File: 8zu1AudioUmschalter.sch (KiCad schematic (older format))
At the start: 56 parts, among them IC1 ATMEGA8A-A, IC2 MAX9890, J1 USB, J2 LUM 1503-07, J3 LUM 1503-07, J4 LUM 1503-07, J5 LUM 1503-07, J6 LUM 1503-07, J7 LUM 1503-07, J8 LUM 1503-07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

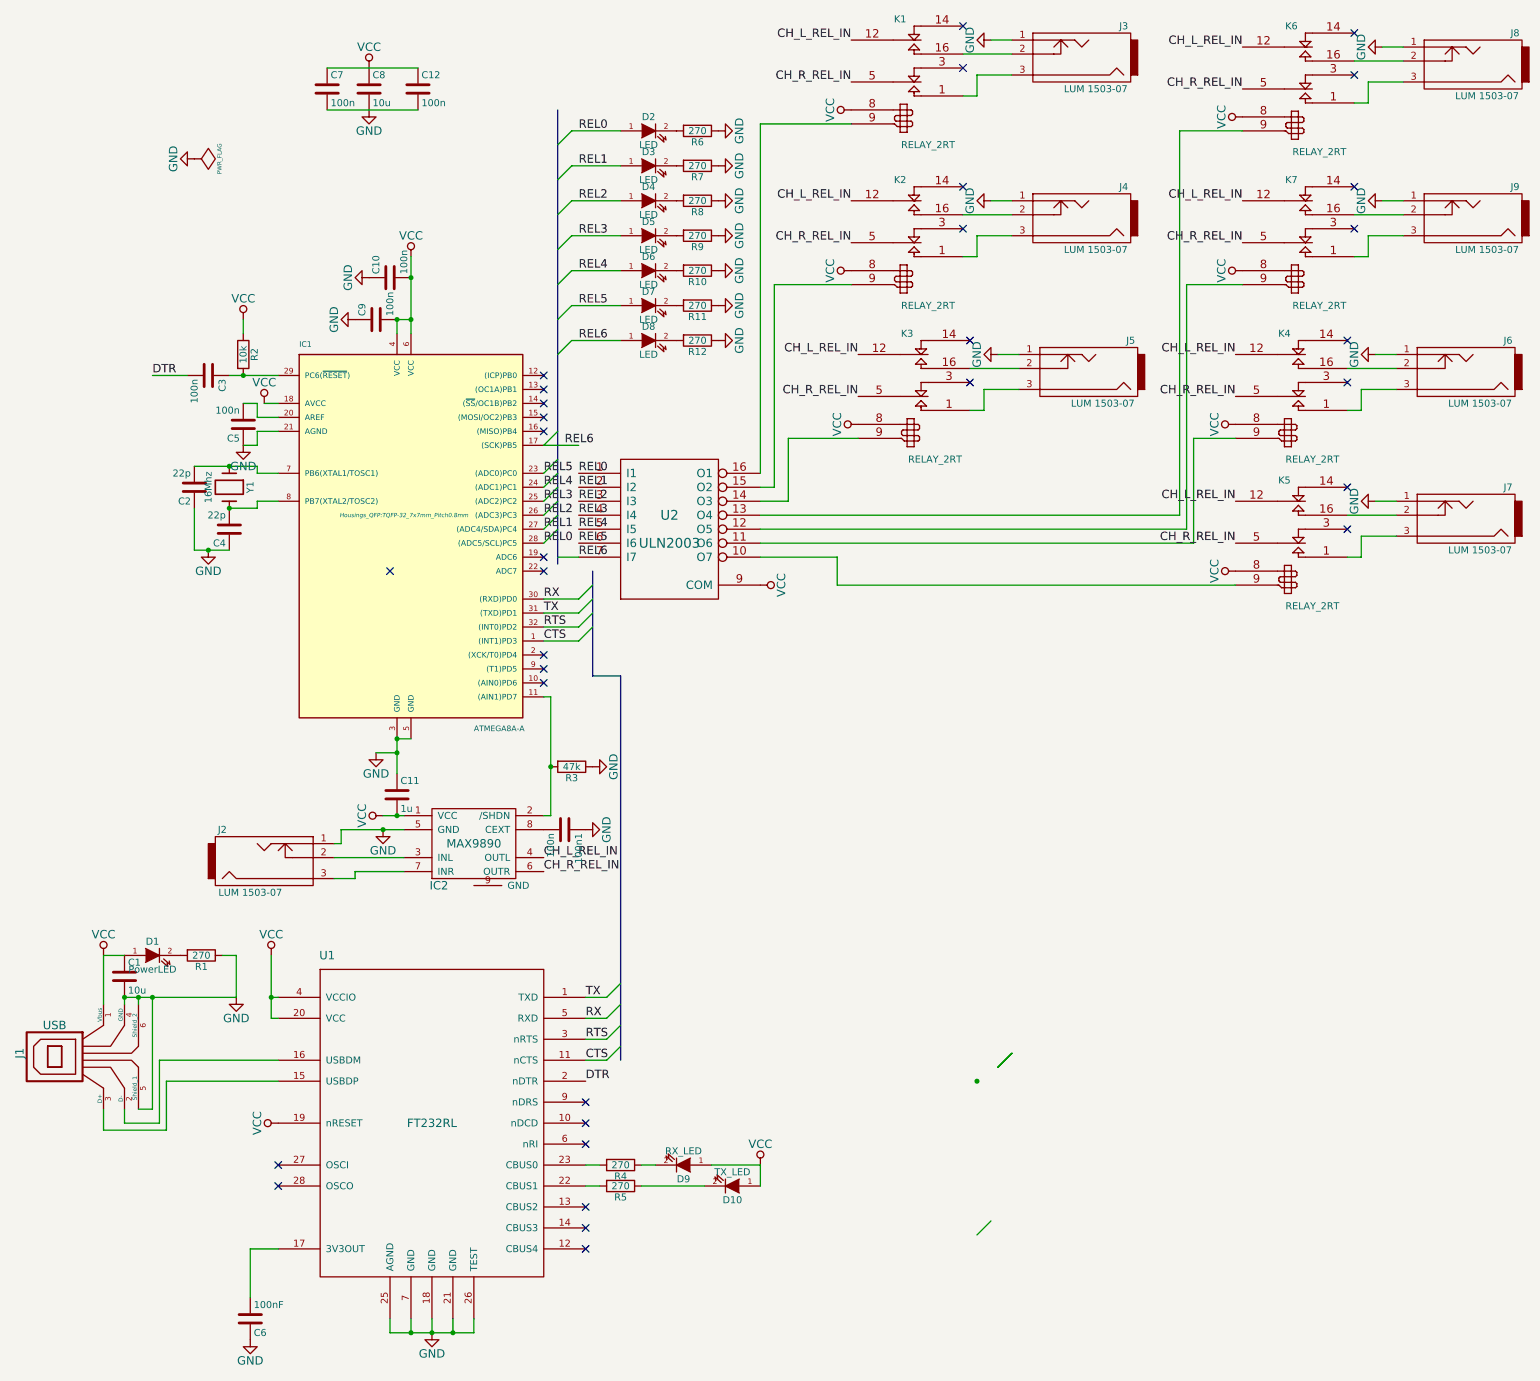
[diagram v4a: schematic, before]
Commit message: Masseflächen dazu
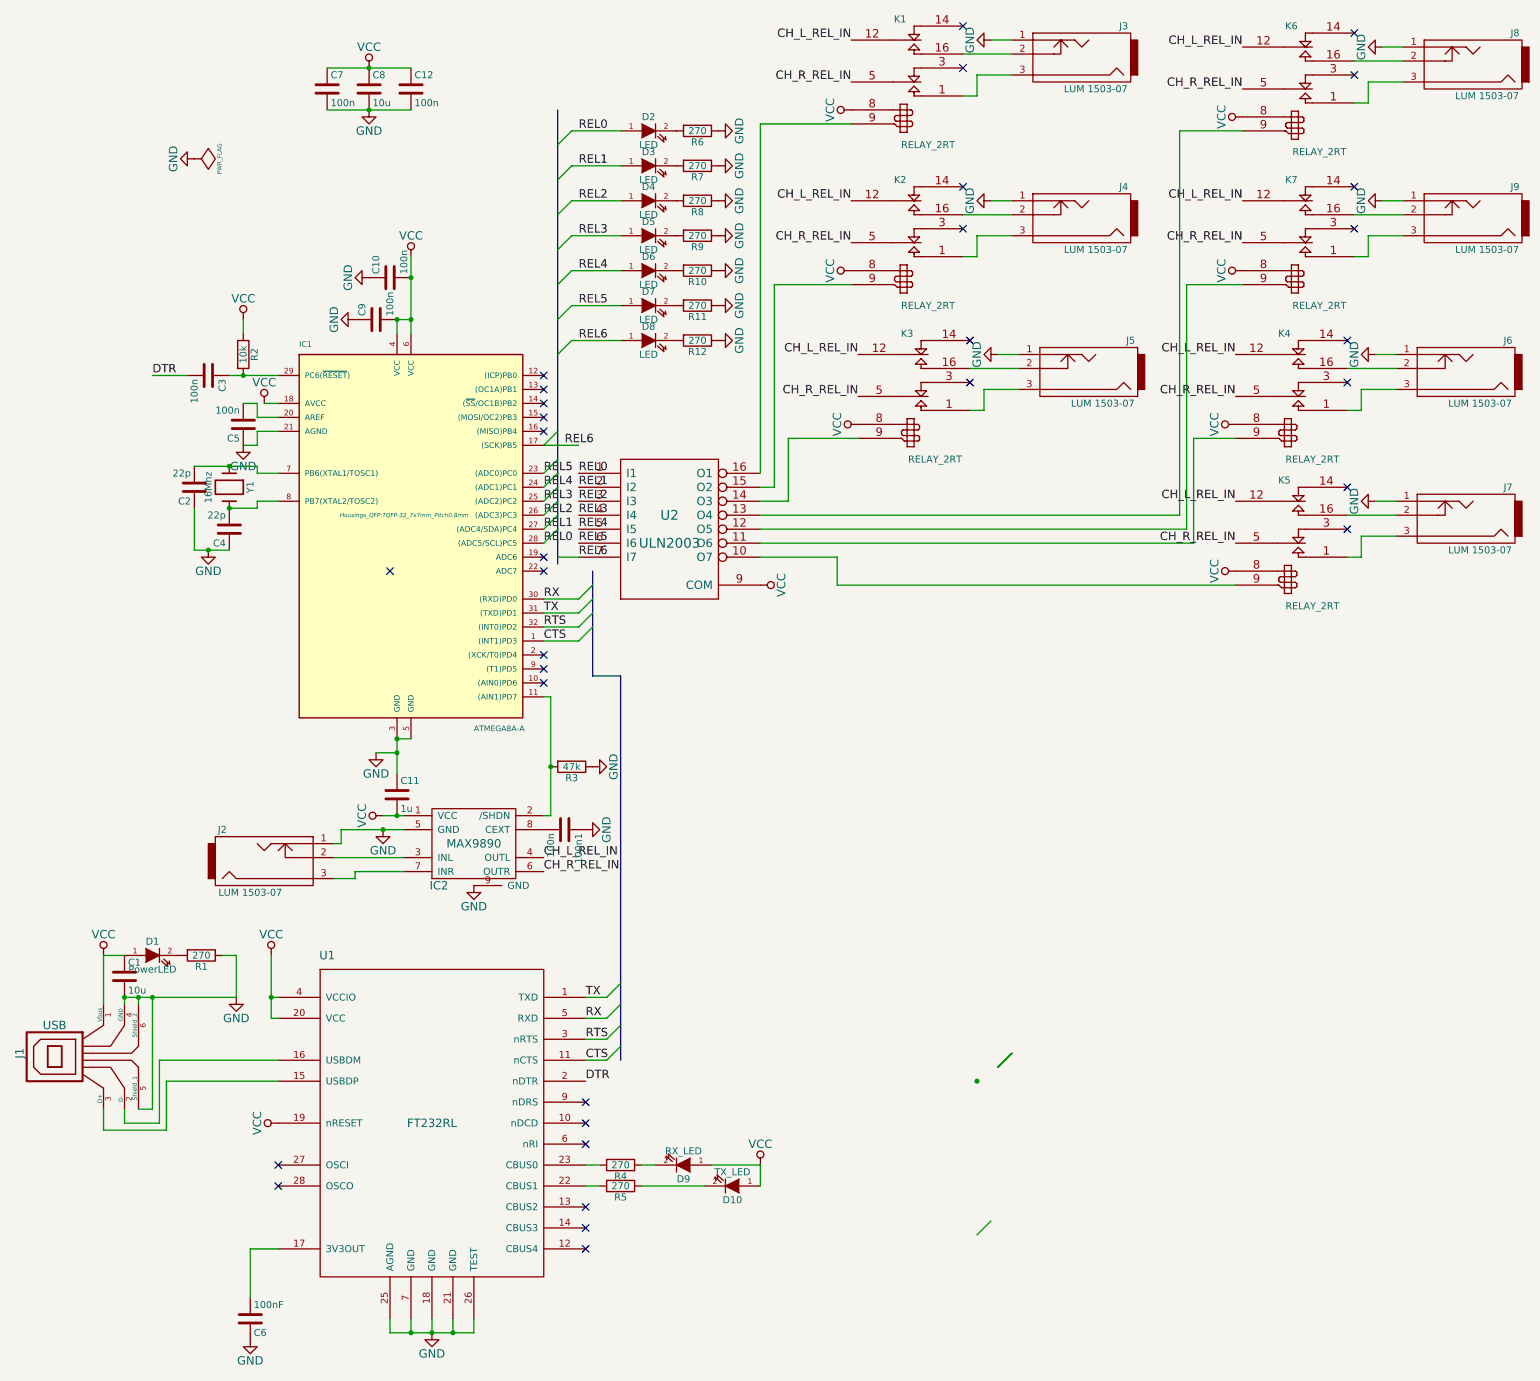
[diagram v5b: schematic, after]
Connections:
- net GND: now also C12.2, C7.2, IC2.9 (GND)
- net VCC: now also C12.1, C7.1
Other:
- moved on the sheet: C12
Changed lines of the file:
@@
 	8300 6750 8250 6750
 Wire Wire Line
-	8300 5900 8300 6750
+	8300 5900 8300 6400
+Wire Wire Line
+	8300 6400 8300 6750
 Wire Wire Line
 	8300 5900 8250 5900
@@
 	9800 9250 9800 9400
 Wire Bus Line
-	8800 5750 8800 8500
+	8800 5750 8800 7950
+Wire Bus Line
+	8800 7950 8800 8100
+Wire Bus Line
+	8800 8100 8800 8250
+Wire Bus Line
+	8800 8250 8800 8400
+Wire Bus Line
+	8800 8400 8800 8500
 Entry Wire Line
 	8700 8050 8800 7950
@@
 	8250 5500 8500 5500
 Wire Bus Line
-	8600 5000 8600 5750
+	8600 5000 8600 5100
+Wire Bus Line
+	8600 5100 8600 5200
+Wire Bus Line
+	8600 5200 8600 5300
+Wire Bus Line
+	8600 5300 8600 5400
+Wire Bus Line
+	8600 5400 8600 5750
 Wire Bus Line
 	8600 5750 8800 5750
@@
 L C C12
 U 1 1 5504C895
-P 7350 1550
-F 0 "C12" H 7375 1650 50  0000 L CNN
-F 1 "100n" H 7375 1450 50  0000 L CNN
-F 2 "Capacitors_SMD:C_0603" H 7388 1400 30  0001 C CNN
-F 3 "" H 7350 1550 60  0000 C CNN
-	1    7350 1550
+P 7300 1550
+F 0 "C12" H 7325 1650 50  0000 L CNN
+F 1 "100n" H 7325 1450 50  0000 L CNN
+F 2 "Capacitors_SMD:C_0603" H 7338 1400 30  0001 C CNN
+F 3 "" H 7300 1550 60  0000 C CNN
+	1    7300 1550
 	1    0    0    -1
 $EndComp
@@
 $EndComp
 Wire Wire Line
-	6700 1700 7350 1700
-Wire Wire Line
-	7350 1400 6700 1400
+	6700 1700 7300 1700
+Wire Wire Line
+	7300 1400 6700 1400
 $Comp
 L GND #PWR07
@@
 	7150 10350 7150 10450
 Wire Wire Line
-	7150 10450 7750 10450
+	7150 10450 7300 10450
+Wire Wire Line
+	7300 10450 7450 10450
+Wire Wire Line
+	7450 10450 7600 10450
+Wire Wire Line
+	7600 10450 7750 10450
 Wire Wire Line
 	7300 10450 7300 10350
@@
 	6100 3300 6100 3200
 Wire Wire Line
-	6000 3600 6350 3600
+	6000 3600 6100 3600
+Wire Wire Line
+	6100 3600 6350 3600
 Connection ~ 6100 3600
 $Comp
@@
 	6200 4300 6200 4250
 Wire Wire Line
-	6200 4250 5750 4250
+	6200 4250 6000 4250
+Wire Wire Line
+	6000 4250 5750 4250
 Wire Wire Line
 	6350 4500 6200 4500
@@
 	6200 4500 6200 4550
 Wire Wire Line
-	6800 6850 7250 6850
+	6800 6850 7100 6850
+Wire Wire Line
+	7100 6850 7250 6850
 $Comp
 L GND #PWR017
@@
 	7200 3200 7200 3300
 Wire Wire Line
-	7300 2750 7300 3300
+	7300 2750 7300 2900
+Wire Wire Line
+	7300 2900 7300 3200
+Wire Wire Line
+	7300 3200 7300 3300
 Wire Wire Line
 	7200 3200 7300 3200
@@
 	6350 8050 6300 8050
 Wire Wire Line
-	6300 7750 6300 8200
+	6300 7750 6300 8050
+Wire Wire Line
+	6300 8050 6300 8200
 NoConn ~ 8250 3800
 NoConn ~ 8250 3700
@@
 	8250 4300 8350 4200
 Wire Bus Line
-	8350 1700 8350 4950
+	8350 1700 8350 1950
+Wire Bus Line
+	8350 1950 8350 2200
+Wire Bus Line
+	8350 2200 8350 2450
+Wire Bus Line
+	8350 2450 8350 2700
+Wire Bus Line
+	8350 2700 8350 2950
+Wire Bus Line
+	8350 2950 8350 3200
+Wire Bus Line
+	8350 3200 8350 3450
+Wire Bus Line
+	8350 3450 8350 4000
+Wire Bus Line
+	8350 4000 8350 4200
+Wire Bus Line
+	8350 4200 8350 4300
+Wire Bus Line
+	8350 4300 8350 4400
+Wire Bus Line
+	8350 4400 8350 4500
+Wire Bus Line
+	8350 4500 8350 4600
+Wire Bus Line
+	8350 4600 8350 4700
+Wire Bus Line
+	8350 4700 8350 4950
 Text Label 8500 4300 0    60   ~ 0
 REL0
@@
 $EndComp
 Wire Wire Line
-	7100 6750 7250 6750
+	7100 6750 7200 6750
+Wire Wire Line
+	7200 6750 7250 6750
 Connection ~ 7200 6750
 Wire Wire Line
@@
 Connection ~ 8300 6400
 Wire Wire Line
-	5750 4850 6000 4850
+	5750 4850 5850 4850
+Wire Wire Line
+	5850 4850 6000 4850
 Wire Wire Line
 	5750 4850 5750 4550
@@
 	6050 7750 6050 8050
 Wire Wire Line
-	6050 8050 5250 8050
+	6050 8050 5450 8050
+Wire Wire Line
+	5450 8050 5350 8050
+Wire Wire Line
+	5350 8050 5250 8050
 Connection ~ 5350 8050
 Connection ~ 5250 8050
@@
 	5100 9000 5100 8850
 Wire Wire Line
-	7200 6450 7200 6200
+	7200 6450 7200 6300
+Wire Wire Line
+	7200 6300 7200 6200
 Wire Wire Line
 	7050 6300 7200 6300
@@
 Text Label 8250 4800 0    60   ~ 0
 REL0
+$Comp
+L GND #PWR046
+U 1 1 5508940B
+P 7750 7250
+F 0 "#PWR046" H 7750 7000 60  0001 C CNN
+F 1 "GND" H 7750 7100 60  0000 C CNN
+F 2 "" H 7750 7250 60  0000 C CNN
+F 3 "" H 7750 7250 60  0000 C CNN
+	1    7750 7250
+	1    0    0    -1
+$EndComp
+Connection ~ 7000 1700
+Connection ~ 7000 1400
 $EndSCHEMATC

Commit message: Platine nun 59 x 80 um den Abstand zwischen den 3.5 mm Buchsen zu vergrößern
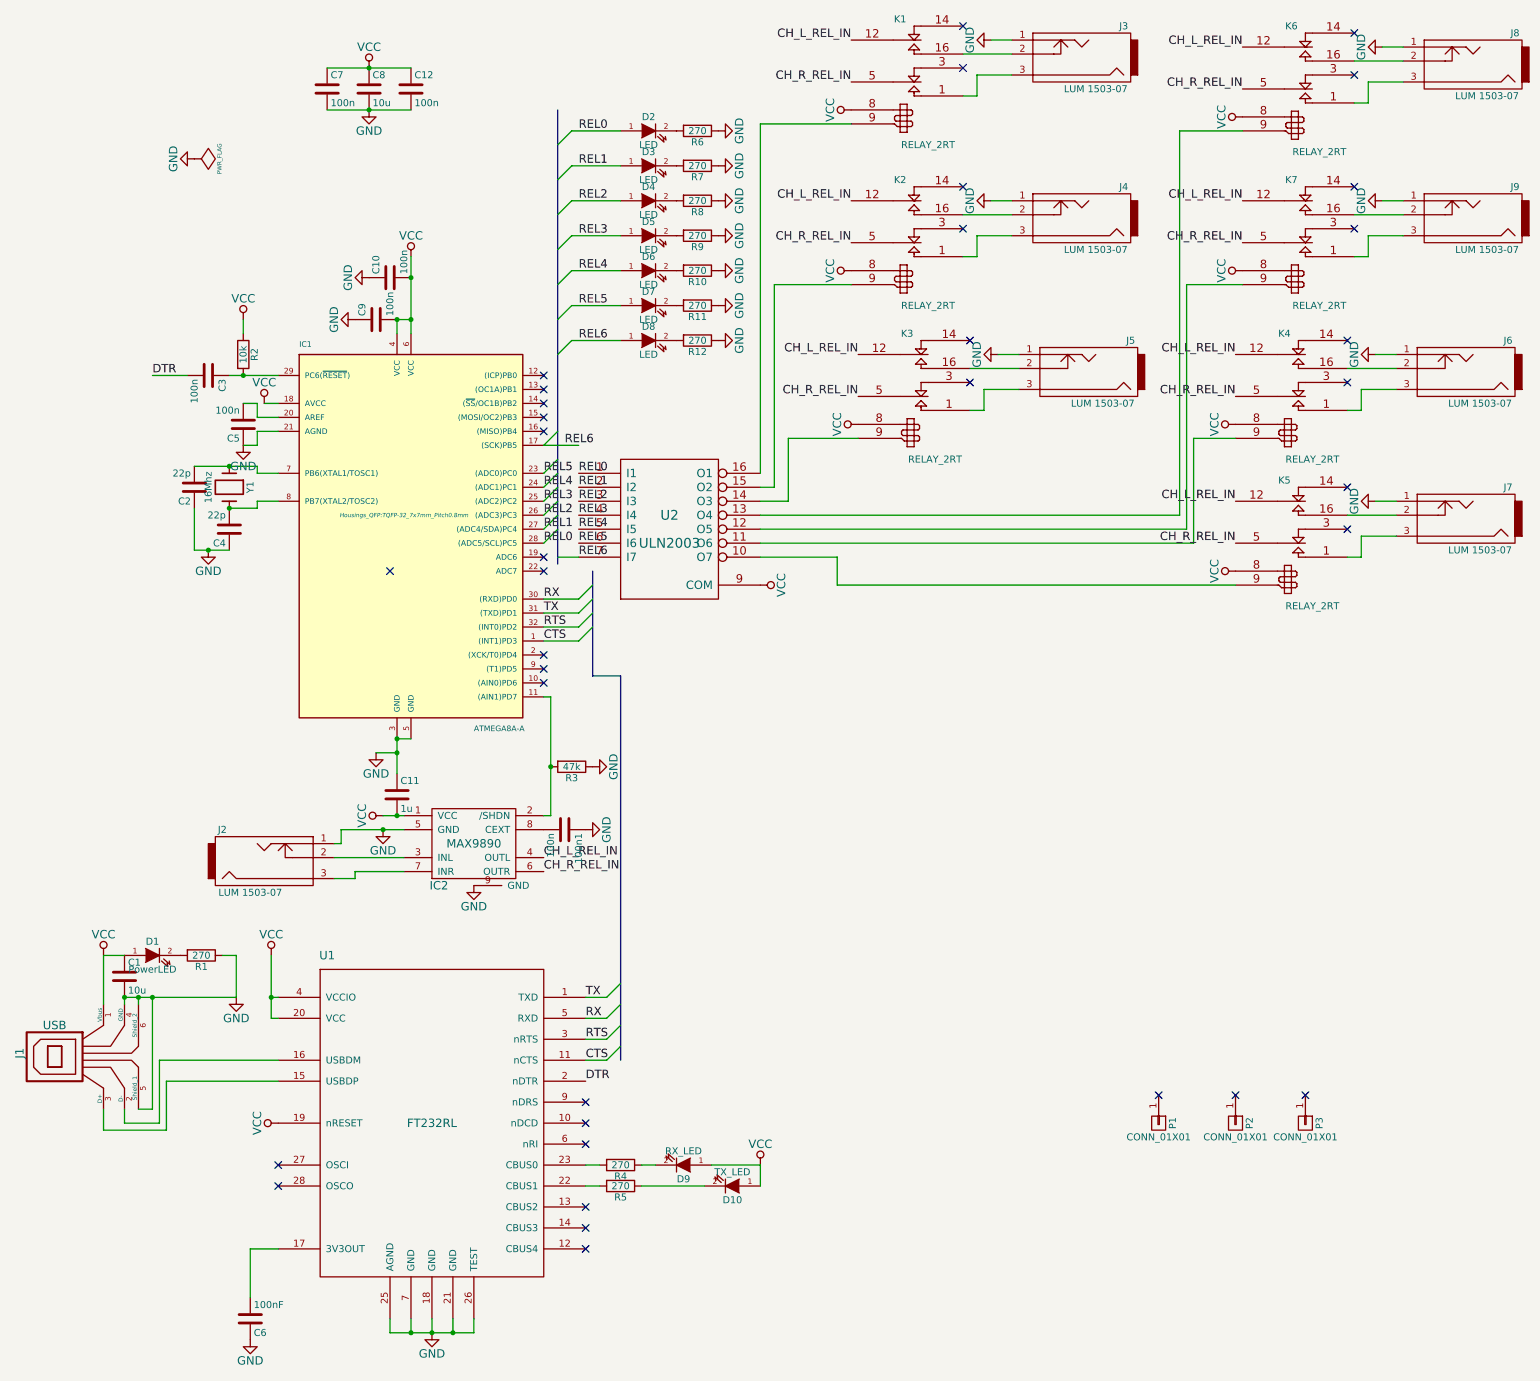
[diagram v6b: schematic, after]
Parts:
- added P1, P2, P3: CONN_01X01, Mounting_Holes:MountingHole_3mm, symbol CONN_01X01
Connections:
- no-connect marks 33 -> 36
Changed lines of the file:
@@
 	8300 6750 8250 6750
 Wire Wire Line
-	8300 5900 8300 6400
-Wire Wire Line
-	8300 6400 8300 6750
+	8300 5900 8300 6750
 Wire Wire Line
 	8300 5900 8250 5900
@@
 	9800 9250 9800 9400
 Wire Bus Line
-	8800 5750 8800 7950
-Wire Bus Line
-	8800 7950 8800 8100
-Wire Bus Line
-	8800 8100 8800 8250
-Wire Bus Line
-	8800 8250 8800 8400
-Wire Bus Line
-	8800 8400 8800 8500
+	8800 5750 8800 8500
 Entry Wire Line
 	8700 8050 8800 7950
@@
 	8250 5500 8500 5500
 Wire Bus Line
-	8600 5000 8600 5100
-Wire Bus Line
-	8600 5100 8600 5200
-Wire Bus Line
-	8600 5200 8600 5300
-Wire Bus Line
-	8600 5300 8600 5400
-Wire Bus Line
-	8600 5400 8600 5750
+	8600 5000 8600 5750
 Wire Bus Line
 	8600 5750 8800 5750
@@
 	7150 10350 7150 10450
 Wire Wire Line
-	7150 10450 7300 10450
-Wire Wire Line
-	7300 10450 7450 10450
-Wire Wire Line
-	7450 10450 7600 10450
-Wire Wire Line
-	7600 10450 7750 10450
+	7150 10450 7750 10450
 Wire Wire Line
 	7300 10450 7300 10350
@@
 	6100 3300 6100 3200
 Wire Wire Line
-	6000 3600 6100 3600
-Wire Wire Line
-	6100 3600 6350 3600
+	6000 3600 6350 3600
 Connection ~ 6100 3600
 $Comp
@@
 	6200 4300 6200 4250
 Wire Wire Line
-	6200 4250 6000 4250
-Wire Wire Line
-	6000 4250 5750 4250
+	6200 4250 5750 4250
 Wire Wire Line
 	6350 4500 6200 4500
@@
 	6200 4500 6200 4550
 Wire Wire Line
-	6800 6850 7100 6850
-Wire Wire Line
-	7100 6850 7250 6850
+	6800 6850 7250 6850
 $Comp
 L GND #PWR017
@@
 	7200 3200 7200 3300
 Wire Wire Line
-	7300 2750 7300 2900
-Wire Wire Line
-	7300 2900 7300 3200
-Wire Wire Line
-	7300 3200 7300 3300
+	7300 2750 7300 3300
 Wire Wire Line
 	7200 3200 7300 3200
@@
 	6350 8050 6300 8050
 Wire Wire Line
-	6300 7750 6300 8050
-Wire Wire Line
-	6300 8050 6300 8200
+	6300 7750 6300 8200
 NoConn ~ 8250 3800
 NoConn ~ 8250 3700
@@
 	8250 4300 8350 4200
 Wire Bus Line
-	8350 1700 8350 1950
-Wire Bus Line
-	8350 1950 8350 2200
-Wire Bus Line
-	8350 2200 8350 2450
-Wire Bus Line
-	8350 2450 8350 2700
-Wire Bus Line
-	8350 2700 8350 2950
-Wire Bus Line
-	8350 2950 8350 3200
-Wire Bus Line
-	8350 3200 8350 3450
-Wire Bus Line
-	8350 3450 8350 4000
-Wire Bus Line
-	8350 4000 8350 4200
-Wire Bus Line
-	8350 4200 8350 4300
-Wire Bus Line
-	8350 4300 8350 4400
-Wire Bus Line
-	8350 4400 8350 4500
-Wire Bus Line
-	8350 4500 8350 4600
-Wire Bus Line
-	8350 4600 8350 4700
-Wire Bus Line
-	8350 4700 8350 4950
+	8350 1700 8350 4950
 Text Label 8500 4300 0    60   ~ 0
 REL0
@@
 $EndComp
 Wire Wire Line
-	7100 6750 7200 6750
-Wire Wire Line
-	7200 6750 7250 6750
+	7100 6750 7250 6750
 Connection ~ 7200 6750
 Wire Wire Line
@@
 Connection ~ 8300 6400
 Wire Wire Line
-	5750 4850 5850 4850
-Wire Wire Line
-	5850 4850 6000 4850
+	5750 4850 6000 4850
 Wire Wire Line
 	5750 4850 5750 4550
@@
 	6050 7750 6050 8050
 Wire Wire Line
-	6050 8050 5450 8050
-Wire Wire Line
-	5450 8050 5350 8050
-Wire Wire Line
-	5350 8050 5250 8050
+	6050 8050 5250 8050
 Connection ~ 5350 8050
 Connection ~ 5250 8050
@@
 	5100 9000 5100 8850
 Wire Wire Line
-	7200 6450 7200 6300
-Wire Wire Line
-	7200 6300 7200 6200
+	7200 6200 7200 6450
 Wire Wire Line
 	7050 6300 7200 6300
 Connection ~ 7200 6300
 Connection ~ 7200 6200
-Connection ~ 11350 8650
-Entry Wire Line
-	11500 8550 11600 8450
-Entry Wire Line
-	11500 8550 11600 8450
-Entry Wire Line
-	11500 8550 11600 8450
-Entry Wire Line
-	11350 9750 11450 9650
 $Comp
 L FT232RL U1
@@
 Connection ~ 7000 1700
 Connection ~ 7000 1400
+$Comp
+L CONN_01X01 P1
+U 1 1 5508A7D3
+P 12650 8950
+F 0 "P1" H 12650 9050 50  0000 C CNN
+F 1 "CONN_01X01" V 12750 8950 50  0000 C CNN
+F 2 "Mounting_Holes:MountingHole_3mm" H 12650 8950 60  0001 C CNN
+F 3 "" H 12650 8950 60  0000 C CNN
+	1    12650 8950
+	0    1    1    0
+$EndComp
+NoConn ~ 12650 8750
+$Comp
+L CONN_01X01 P2
+U 1 1 5508BB0F
+P 13200 8950
+F 0 "P2" H 13200 9050 50  0000 C CNN
+F 1 "CONN_01X01" V 13300 8950 50  0000 C CNN
+F 2 "Mounting_Holes:MountingHole_3mm" H 13200 8950 60  0001 C CNN
+F 3 "" H 13200 8950 60  0000 C CNN
+	1    13200 8950
+	0    1    1    0
+$EndComp
+NoConn ~ 13200 8750
+$Comp
+L CONN_01X01 P3
+U 1 1 5508BBA1
+P 13700 8950
+F 0 "P3" H 13700 9050 50  0000 C CNN
+F 1 "CONN_01X01" V 13800 8950 50  0000 C CNN
+F 2 "Mounting_Holes:MountingHole_3mm" H 13700 8950 60  0001 C CNN
+F 3 "" H 13700 8950 60  0000 C CNN
+	1    13700 8950
+	0    1    1    0
+$EndComp
+NoConn ~ 13700 8750
 $EndSCHEMATC
